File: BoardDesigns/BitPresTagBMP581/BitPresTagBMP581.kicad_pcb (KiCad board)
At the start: 4 copper layers, 18 x 10 mm, 26 parts, among them J201 CONN_02X04, J301 Conn_01x01, J302 Conn_01x01, J303 Conn_01x01, J304 Conn_01x01, J401 CONN_01X02, Q501 PMBT2222AMBYL, U1 at25ex321D-UUN, U2 ADXL367BCCZ-RL7, U3 BMP585, U302 stm32l431kc, U501 RV-3028-C8-32.768kHz-1PPM-TA-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

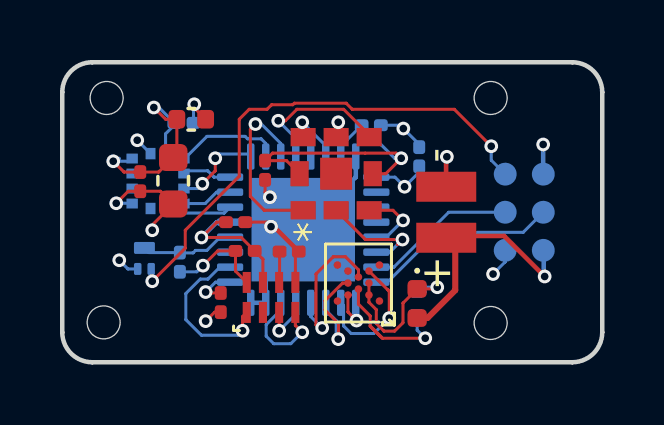
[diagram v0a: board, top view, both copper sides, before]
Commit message: BitPresTagBMP581: design review, and fix the two defects it found
Full kicad-happy review against a fresh analyzer run. The pre-existing
analysis/ was poisoned (project_settings.source named
BitTagNG-LIS2DU12.kicad_pcb-back.kicad_pro, so every rule-derived number
was measured against the wrong rule set); those three flat JSONs are
removed and the run redone.

Design fixes:
  - C8 220nF on U2.9 VREG_OUT. The ADXL367 datasheet requires an external
    0.2uF on this pin; it was a single-pin net.
  - R2 10R in series in the BMP585 supply (PB1 -> R2 -> C3/C5/U3.4/U3.8).
    BMP585 Table 4 footnote a makes this normative: "For supply ramps
    < 0.01 ms, a 10 Ohm resistor must be connected in series to the power
    supply". Decoupling stays on the load side.
  - U3 pin 9 (L/M) no-connect flag. It is the lasermarking pad; the
    datasheet says no external connection is possible (S/R coverage).
  - U2 pins 7/11 GND pin type power_out -> power_in.
  - Rail relabelled +2V5 -> VCC. There is no 2.5V regulator; the rail is
    VBAT less a Schottky drop and tracks the cell (~3.1V to ~1.9V). VIN
    global labels kept as the environment-facing alias, so the netlist and
    PCB net name are unchanged.

Design rules tightened: edge clearance 0 -> 0.3mm, annular ring 0.1016 ->
0.1524mm, vias 0.5048/0.2mm, and track_not_centered_on_via re-enabled.

Verified: KiCad DRC 0 violations / 0 unconnected, KiCad ERC 0 violations
(was 6), padnet_crosscheck 28 footprints / 0 mismatches. Pinouts verified
against manufacturer PDFs for Q501 (PMBT2222AMB), U1 (AT25XE321D 12-ball
WLCSP), U2 (ADXL367), U3 (BMP585) and U501 (RV-3028 backup network).

.kicad-happy.json rewritten: the previous one had been copied from a
CompassTag-style board and described an AK09940A, a TPS7A2018 at U4 and a
+1V8 rail, none of which exist here. It now carries the real 33-entry pin
map, 21 evidence-backed suppressions and the firmware contracts.

Co-Authored-By: Claude Opus 5 (1M context) <noreply@anthropic.com>
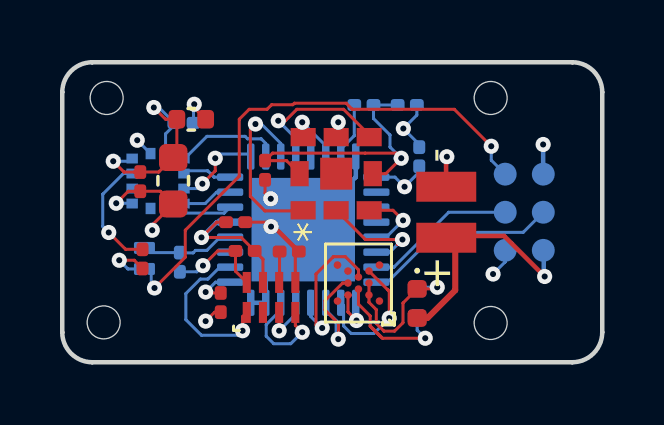
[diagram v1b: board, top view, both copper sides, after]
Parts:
- added C8: 220nf, AccelTag:C_0201_0603Metric, F.Cu at (142.7, 109.6)
- added R2: 10, AccelTag:R_0201_0603Metric, B.Cu at (150.1, 104.4)
- moved C3 1.38 mm to (151.5, 104.4)
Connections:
- C3 pad 1: /LPS_PWR -> Net-(U3-VDD)
- C5 pad 1: /LPS_PWR -> Net-(U3-VDD)
- U2 pad 9: unconnected-(U2-VREG_OUT-Pad9) -> Net-(U2-VREG_OUT)
- U3 pad 4: /LPS_PWR -> Net-(U3-VDD)
- U3 pad 8: /LPS_PWR -> Net-(U3-VDD)
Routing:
- net Net-(U3-VDD): track 0.00 -> 10.4 mm, vias 0 -> 1
- net /LPS_PWR: track 10.4 -> 2.25 mm, vias 1 -> 0
- net Net-(U2-VREG_OUT): track 0.00 -> 3.98 mm, vias 0 -> 1
